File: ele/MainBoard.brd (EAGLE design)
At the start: 136.6 x 100 mm, 114 parts, among them IC1 MCP23017SP, IC2 74HC595D, IC3 74HC595D, X1 POWER_IN, X2 POWER_OUT

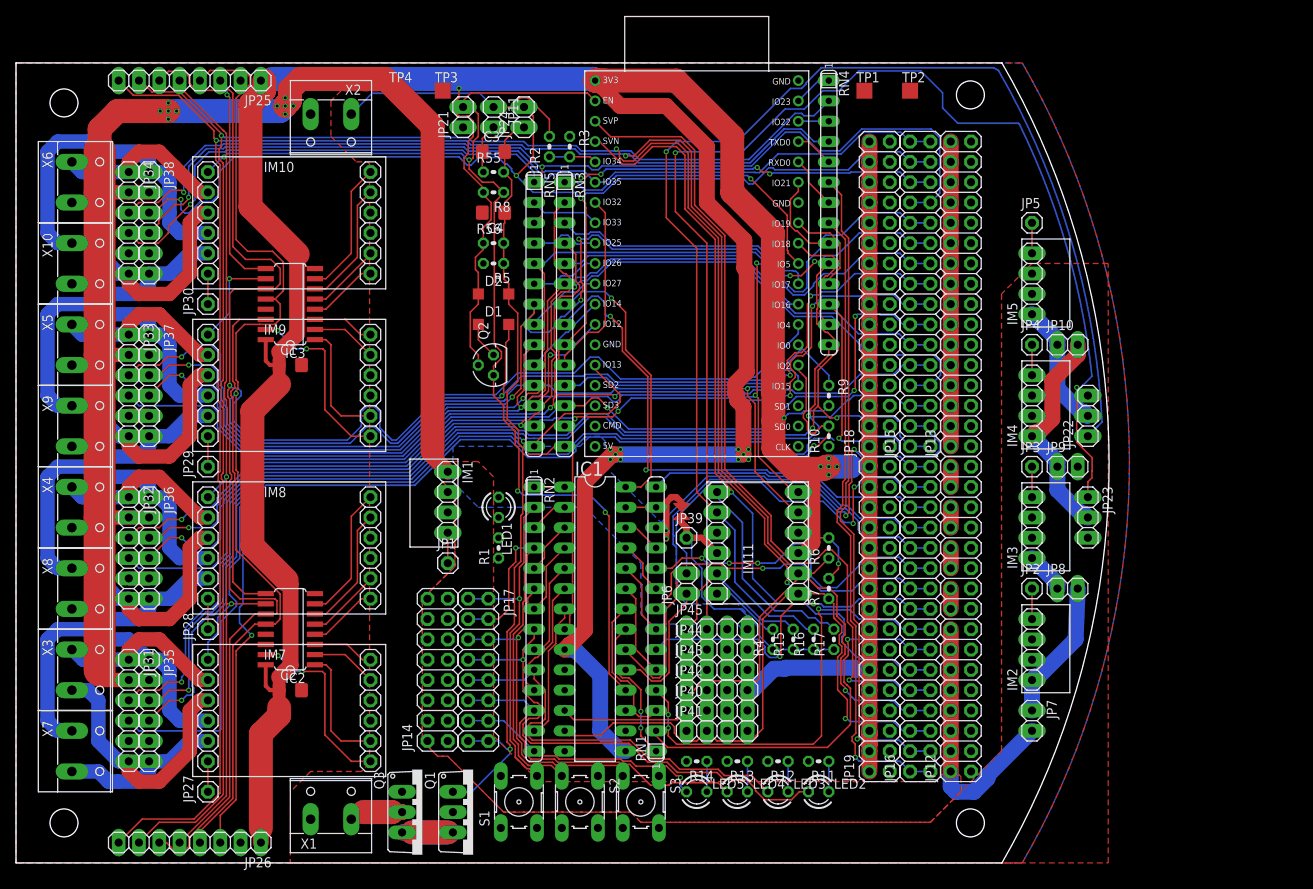
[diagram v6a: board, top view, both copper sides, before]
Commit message: ele: Route much signals. Wow.
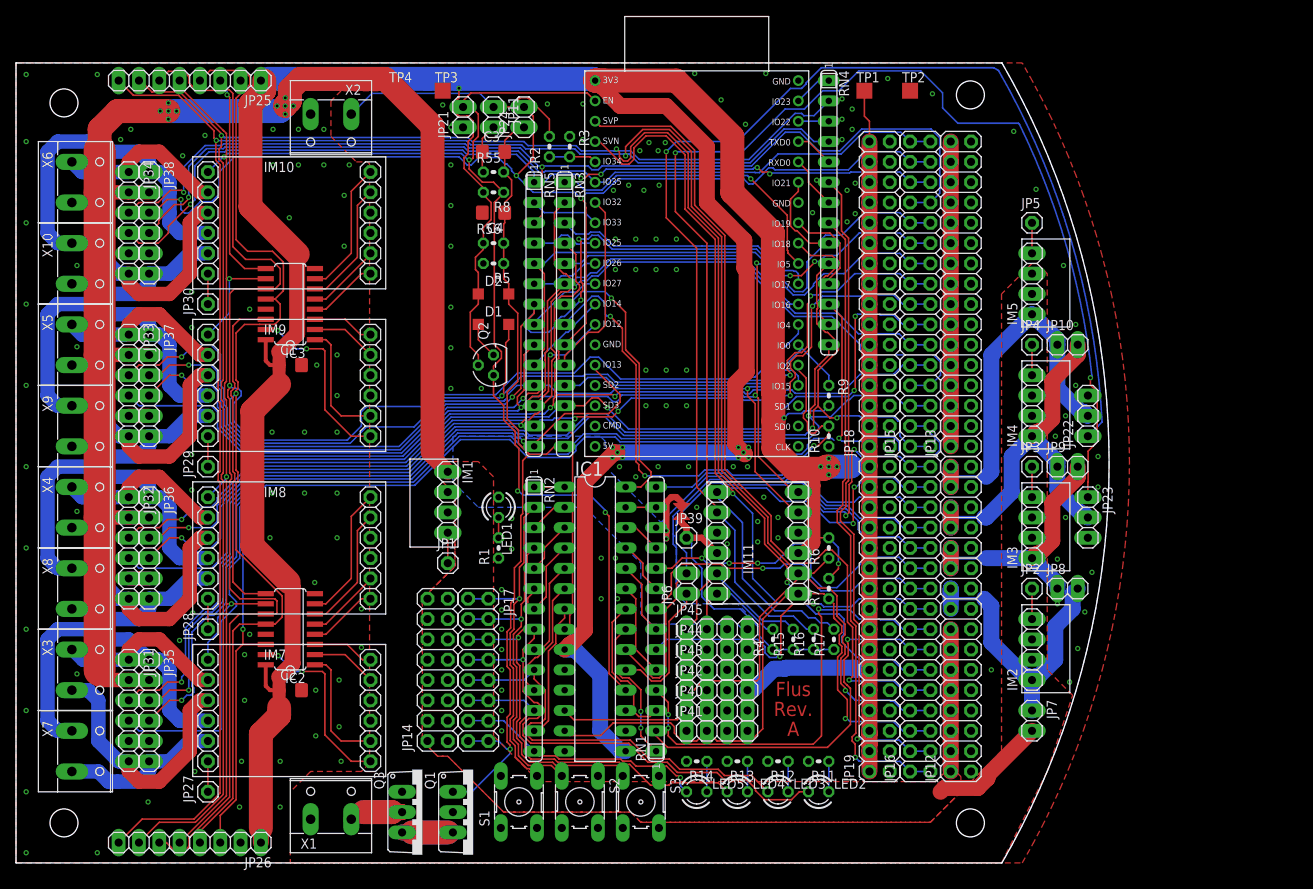
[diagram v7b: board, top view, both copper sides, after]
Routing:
- net 5V_5: track 18.3 -> 48.0 mm
- net 5V_3: track 7.67 -> 34.4 mm
- net 5V_4: track 29.8 -> 49.3 mm
- net 5V_2: track 58.4 -> 76.8 mm
- net EB1: track 49.7 -> 40.7 mm
- net +3V3: track 536.9 -> 544.3 mm
- net SCKMOT: track 223.4 -> 219.9 mm
- net N$9: track 0.00 -> 2.54 mm
- net +5V: track 239.0 -> 241.4 mm
- net EA7: track 67.8 -> 70.1 mm
- net IO39: track 99.2 -> 101.2 mm
- net SDA: track 348.0 -> 349.9 mm
- net SCL: track 343.2 -> 345.0 mm
- net SERMOT: track 142.2 -> 140.8 mm
- net B5V: track 172.7 -> 171.6 mm
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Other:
- board text added: "Flus Rev. A"

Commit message: ele: Release Rev. A RC1
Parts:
- moved JP10 21.3 mm to (121.9, 45.7), turned to 270 degrees
- moved JP7 13.7 mm to (121.9, 30.5)
- moved JP9 13.0 mm to (121.9, 40.6), turned to 270 degrees
- moved JP8 9.61 mm to (121.9, 35.6), turned to 270 degrees
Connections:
- net 5V_2: no longer JP13.10, JP13.12, JP13.14, JP13.16, JP13.18, JP13.2, JP13.20, JP13.22, JP13.24, JP13.26, JP13.28, JP13.30, JP13.32, JP13.4, JP13.6, JP13.8
- net 5V_5: now also JP13.10, JP13.12, JP13.14, JP13.16, JP13.18, JP13.2, JP13.20, JP13.22, JP13.24, JP13.26, JP13.28, JP13.30, JP13.32, JP13.4, JP13.6, JP13.8
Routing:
- net 5V_5: track 48.0 -> 162.8 mm
- net 5V_2: track 76.8 -> 41.7 mm
- net +5V: track 241.4 -> 208.9 mm
- net 5V_4: track 49.3 -> 54.1 mm
- net 5V_3: track 34.4 -> 31.1 mm
- net +3V3: track 544.3 -> 543.4 mm
- net EB3: track 63.1 -> 63.6 mm, vias 1 -> 2
- net GND: vias 161 -> 160
